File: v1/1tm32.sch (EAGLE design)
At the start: 45 parts, among them IC1 STM32L412RBT6P, IC2 BGM240PA32VNN3, J2 10118192-0001LF, J3 FTSH-105-01-L-D, J4 20021321-00020C4LF, SW1 LL3301FF065QJ, U2 LD39050PU33R, Y1 8MHz, Y2 32.7KHz

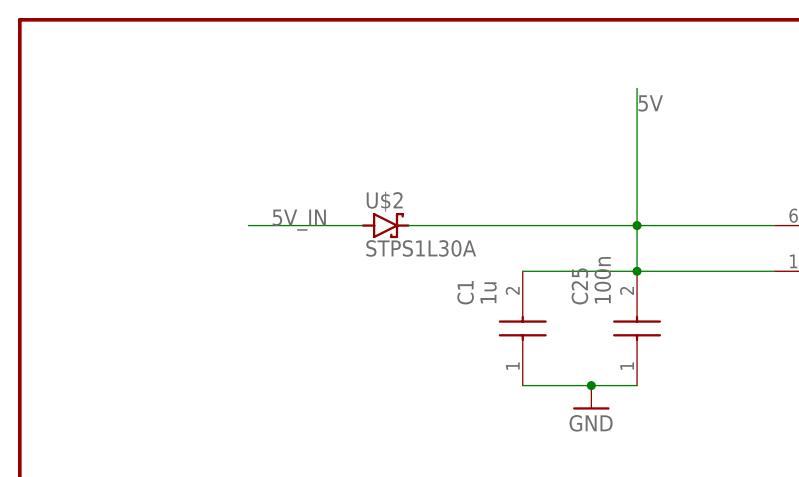
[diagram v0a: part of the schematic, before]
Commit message: updated the Schottky diode to RBR1L30ATE25
datasheet: https://www.mouser.com/datasheet/2/348/ROHM_S_A0008995718_1-2562906.pdf
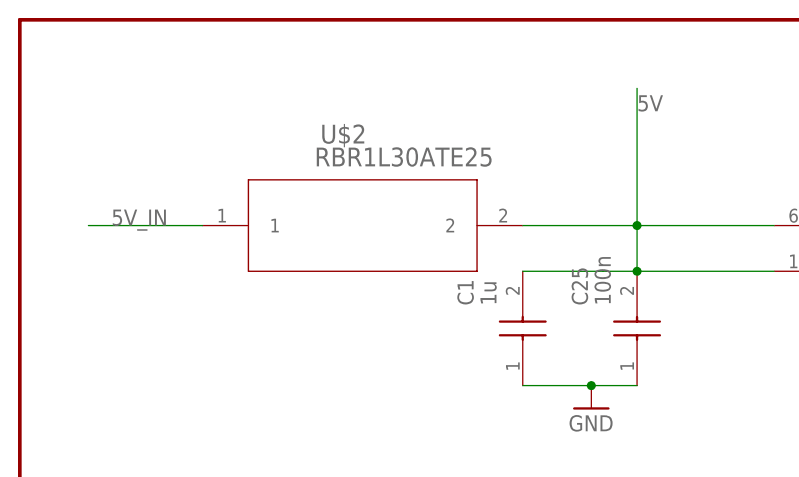
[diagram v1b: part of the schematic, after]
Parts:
- U$2: value STPS1L30A -> RBR1L30ATE25; device ce-capstone:STPS1L30A -> RBR1L30ATE25(scho_diode):RBR1L30ATE25
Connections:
- net 5V: now also U$2.2; no longer U$2.C
- net 5V_IN: now also U$2.1; no longer U$2.A
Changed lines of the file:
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@@
 <part name="U2" library="ce-capstone" deviceset="LD39050PU33R" device=""/>
 <part name="U$1" library="ce-capstone" deviceset="SML-P12VTT86" device="" value="LED_R"/>
-<part name="U$2" library="ce-capstone" deviceset="STPS1L30A" device=""/>
 <part name="GND2" library="supply1" library_urn="urn:adsk.eagle:library:371" deviceset="GND" device=""/>
 <part name="GND3" library="supply1" library_urn="urn:adsk.eagle:library:371" deviceset="GND" device=""/>
@@
 <part name="R5" library="RC0805JR-0710KL" deviceset="RC0805JR-0710KL" device="" value="10K"/>
 <part name="R11" library="RC0805JR-0710KL" deviceset="RC0805JR-0710KL" device="" value="10K"/>
+<part name="U$2" library="RBR1L30ATE25(scho_diode)" deviceset="RBR1L30ATE25" device=""/>
 </parts>
 <sheets>
@@
 <attribute name="VALUE" x="-22.225" y="102.108" size="1.778" layer="96" rot="R90"/>
 </instance>
-<instance part="U$2" gate="G$1" x="-142.24" y="132.08" smashed="yes">
-<attribute name="NAME" x="-144.526" y="133.985" size="1.778" layer="95"/>
-<attribute name="VALUE" x="-144.526" y="128.651" size="1.778" layer="96"/>
-</instance>
 <instance part="GND2" gate="1" x="-119.38" y="111.76" smashed="yes">
 <attribute name="VALUE" x="-121.92" y="109.22" size="1.778" layer="96"/>
@@
 <attribute name="NAME" x="26.67" y="-39.37" size="1.778" layer="95" rot="R90" align="center-left"/>
 <attribute name="VALUE" x="26.67" y="-31.75" size="1.778" layer="96" rot="R90" align="center-left"/>
+</instance>
+<instance part="U$2" gate="A" x="-165.1" y="132.08" smashed="yes">
+<attribute name="NAME" x="-149.5044" y="141.1986" size="2.0828" layer="95" ratio="6" rot="SR0"/>
+<attribute name="VALUE" x="-150.1394" y="138.6586" size="2.0828" layer="96" ratio="6" rot="SR0"/>
 </instance>
 </instances>
@@
 <net name="5V_IN" class="0">
 <segment>
-<pinref part="U$2" gate="G$1" pin="A"/>
-<wire x1="-144.78" y1="132.08" x2="-157.48" y2="132.08" width="0.1524" layer="91"/>
-<label x="-154.94" y="132.08" size="1.778" layer="95"/>
+<wire x1="-162.56" y1="132.08" x2="-175.26" y2="132.08" width="0.1524" layer="91"/>
+<label x="-172.72" y="132.08" size="1.778" layer="95"/>
+<pinref part="U$2" gate="A" pin="1"/>
 </segment>
 <segment>
@@
 <segment>
 <pinref part="U2" gate="G$1" pin="VIN"/>
-<pinref part="U$2" gate="G$1" pin="C"/>
 <wire x1="-99.06" y1="132.08" x2="-114.3" y2="132.08" width="0.1524" layer="91"/>
 <pinref part="U2" gate="G$1" pin="EN"/>
-<wire x1="-114.3" y1="132.08" x2="-139.7" y2="132.08" width="0.1524" layer="91"/>
+<wire x1="-114.3" y1="132.08" x2="-127" y2="132.08" width="0.1524" layer="91"/>
 <wire x1="-127" y1="127" x2="-114.3" y2="127" width="0.1524" layer="91"/>
 <wire x1="-114.3" y1="127" x2="-99.06" y2="127" width="0.1524" layer="91"/>
@@
 <pinref part="C1" gate="G$1" pin="2"/>
 <pinref part="C25" gate="G$1" pin="2"/>
-</segment>
-<segment>
+<pinref part="U$2" gate="A" pin="2"/>
+</segment>
+<segment>

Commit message: changed errors
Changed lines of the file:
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@@
 <pinref part="C39" gate="G$1" pin="2"/>
 <wire x1="-109.22" y1="22.86" x2="-91.44" y2="22.86" width="0.1524" layer="91"/>
+<junction x="-91.44" y="-60.96"/>
 </segment>
 <segment>
